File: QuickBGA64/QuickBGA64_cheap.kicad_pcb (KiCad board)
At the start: 2 copper layers, 17 x 17 mm, 19 parts, among them IC1 EOS-S3-BGA64, J1 TOP, J2 RIGHT, J3 BOTTOM, J4 LEFT, U1 GD25Q16CWIGR, Y1 ECS-_327-12_5-34B-TR

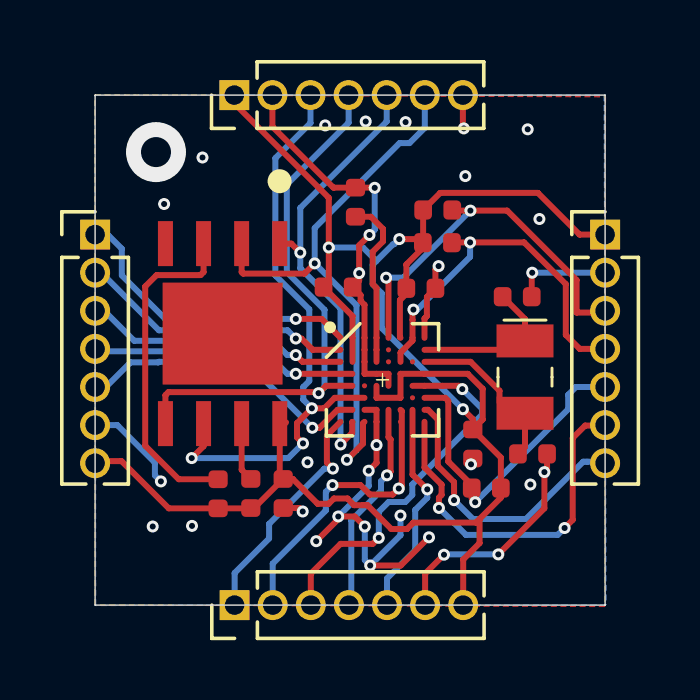
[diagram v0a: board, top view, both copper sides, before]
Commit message: Adding LED, sending to production
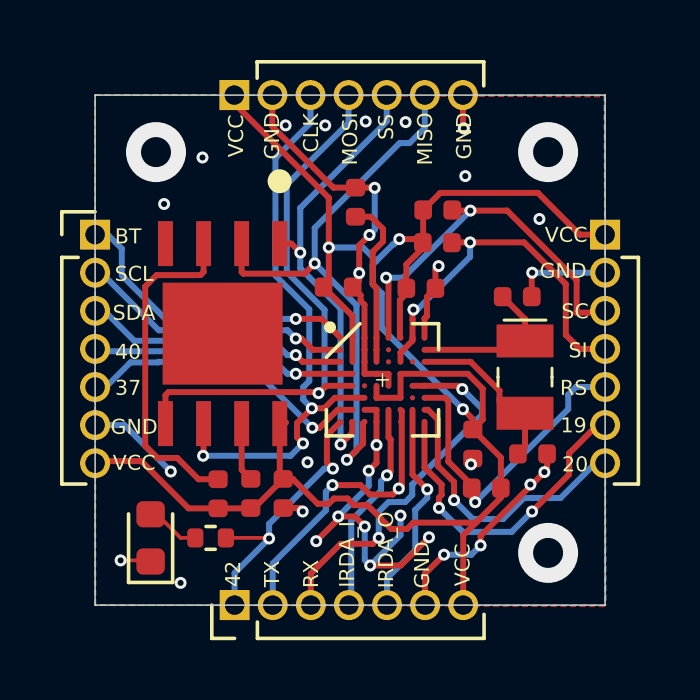
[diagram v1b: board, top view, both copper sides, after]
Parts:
- added D1: LED, LED_SMD:LED_0603_1608Metric, F.Cu at (86.8, 80.5)
- added G***: LOGO, parts:OSH_10x10, B.Cu at (93.4, 74.5)
- added R7: R300, Resistor_SMD:R_0402_1005Metric, F.Cu at (88.8, 80.5)
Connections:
- IC1 pad B5: Net-(IC1-PadB5) -> (no net)
- IC1 pad C5: Net-(IC1-PadC5) -> (no net)
- IC1 pad C7: Net-(IC1-PadC7) -> (no net)
- IC1 pad E3: Net-(IC1-PadE3) -> (no net)
- IC1 pad F7: Net-(IC1-PadF7) -> (no net)
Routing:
- net Net-(D1-Pad2): track 0.00 -> 1.82 mm
- net /42: track 7.63 -> 9.08 mm, vias 1 -> 2
- net /B_19: track 11.9 -> 10.6 mm
- net /CLK: track 19.9 -> 19.3 mm
- net GND: track 43.1 -> 43.6 mm, vias 33 -> 35
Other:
- board text added: "19"
- board text added: "20"
- board text added: "37"
- board text added: "40"
- board text added: "42"
- board text added: "BAT_M"
- board text added: "BT"
- board text added: "B_19"
- board text added: "B_20"
- board text added: "CLK"
- board text added: "GND"
- board text added: "IRDA_I"
- board text added: "IRDA_O"
- board text added: "MISO"
- board text added: "MOSI"
- board text added: "RS"
- board text added: "RST"
- board text added: "RX"
- board text added: "SC"
- board text added: "SCL"
- board text added: "SDA"
- board text added: "SI"
- board text added: "SS"
- board text added: "SWD_CLK"
- board text added: "SWD_IO"
- board text added: "TX"
- board text added: "VCC"
